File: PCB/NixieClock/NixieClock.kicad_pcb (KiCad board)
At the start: 2 copper layers, 1 part, among them U1 ESP32-DEVKITC-32D

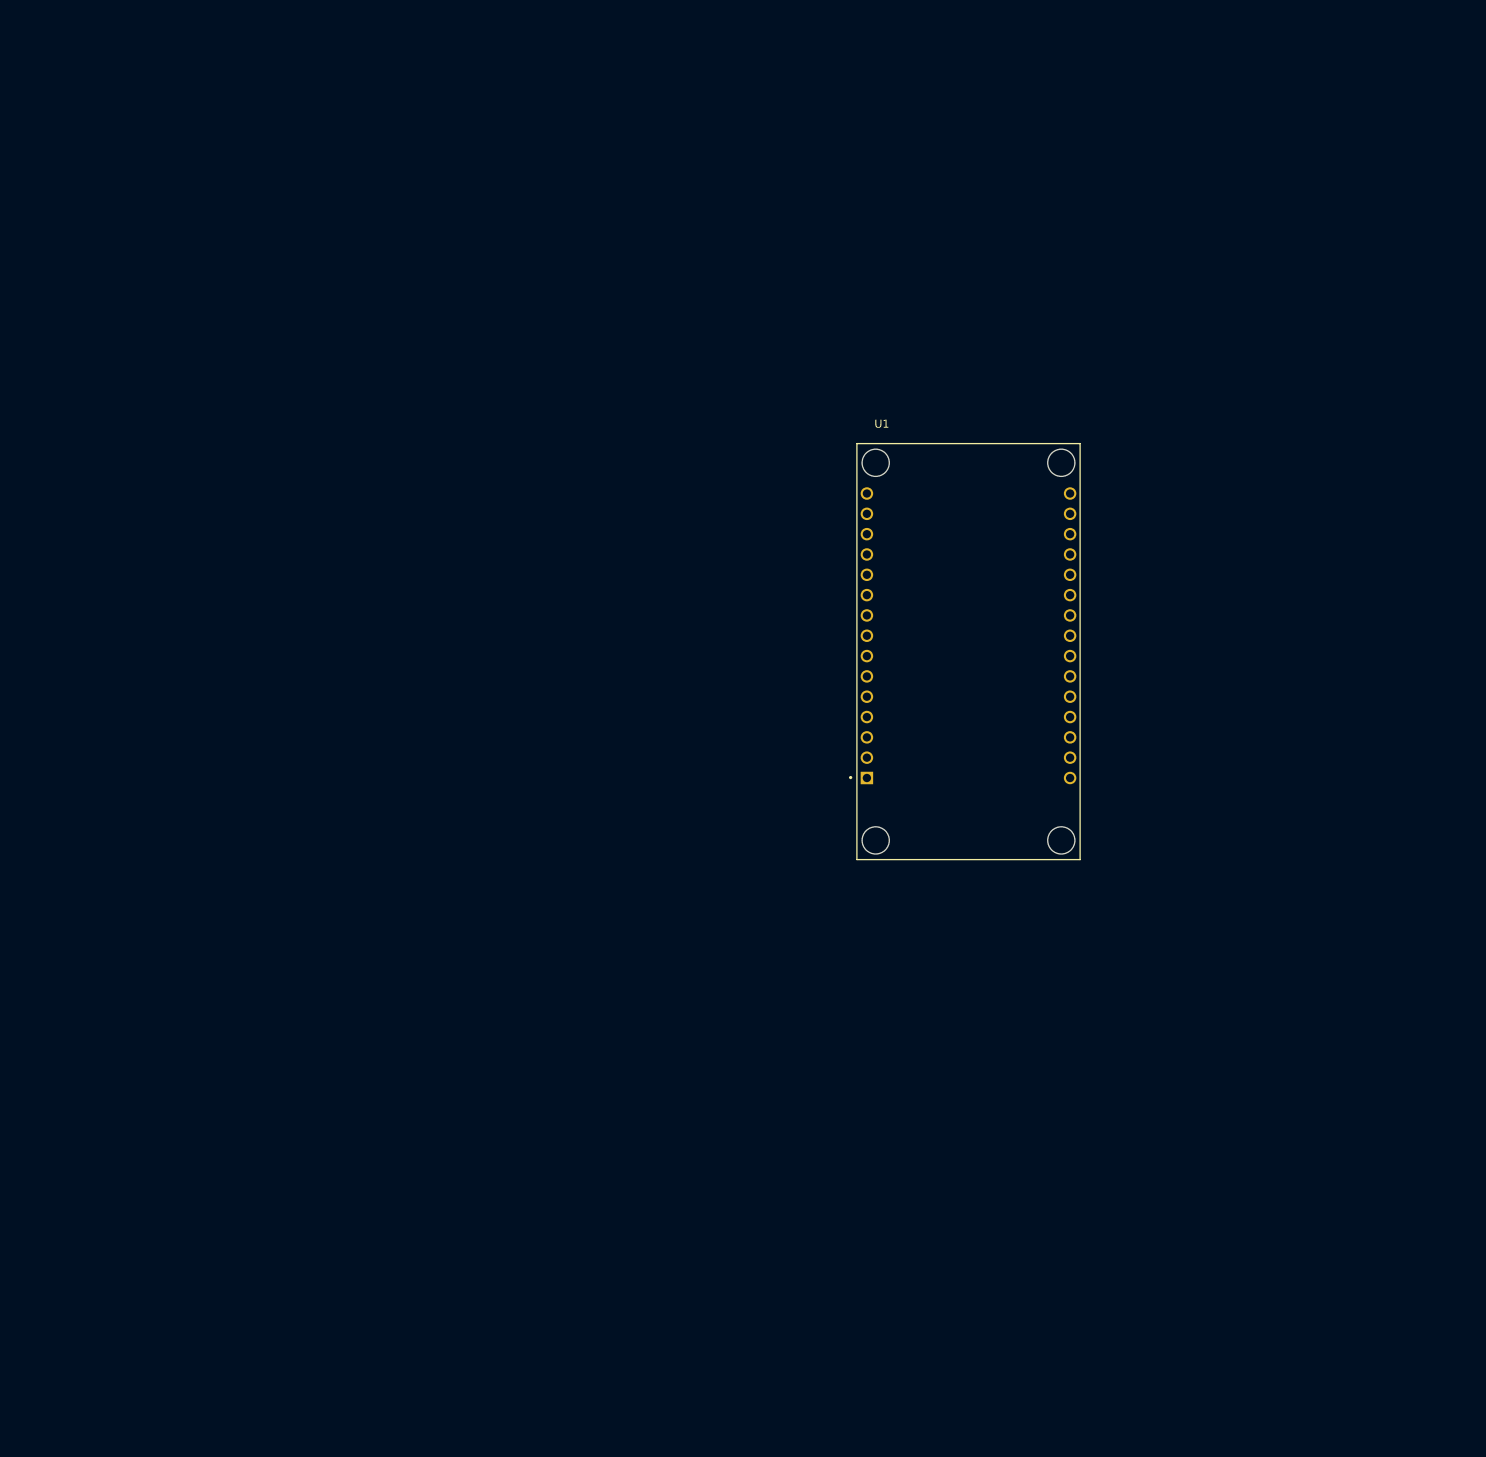
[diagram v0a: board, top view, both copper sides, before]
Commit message: nixie panel PCB layout progress
laid out tube 1 with top and bottom traces. added GND polygon on both sides, with exception zone around tube 1. tubes 2-4 to be laid out with top and bottom traces
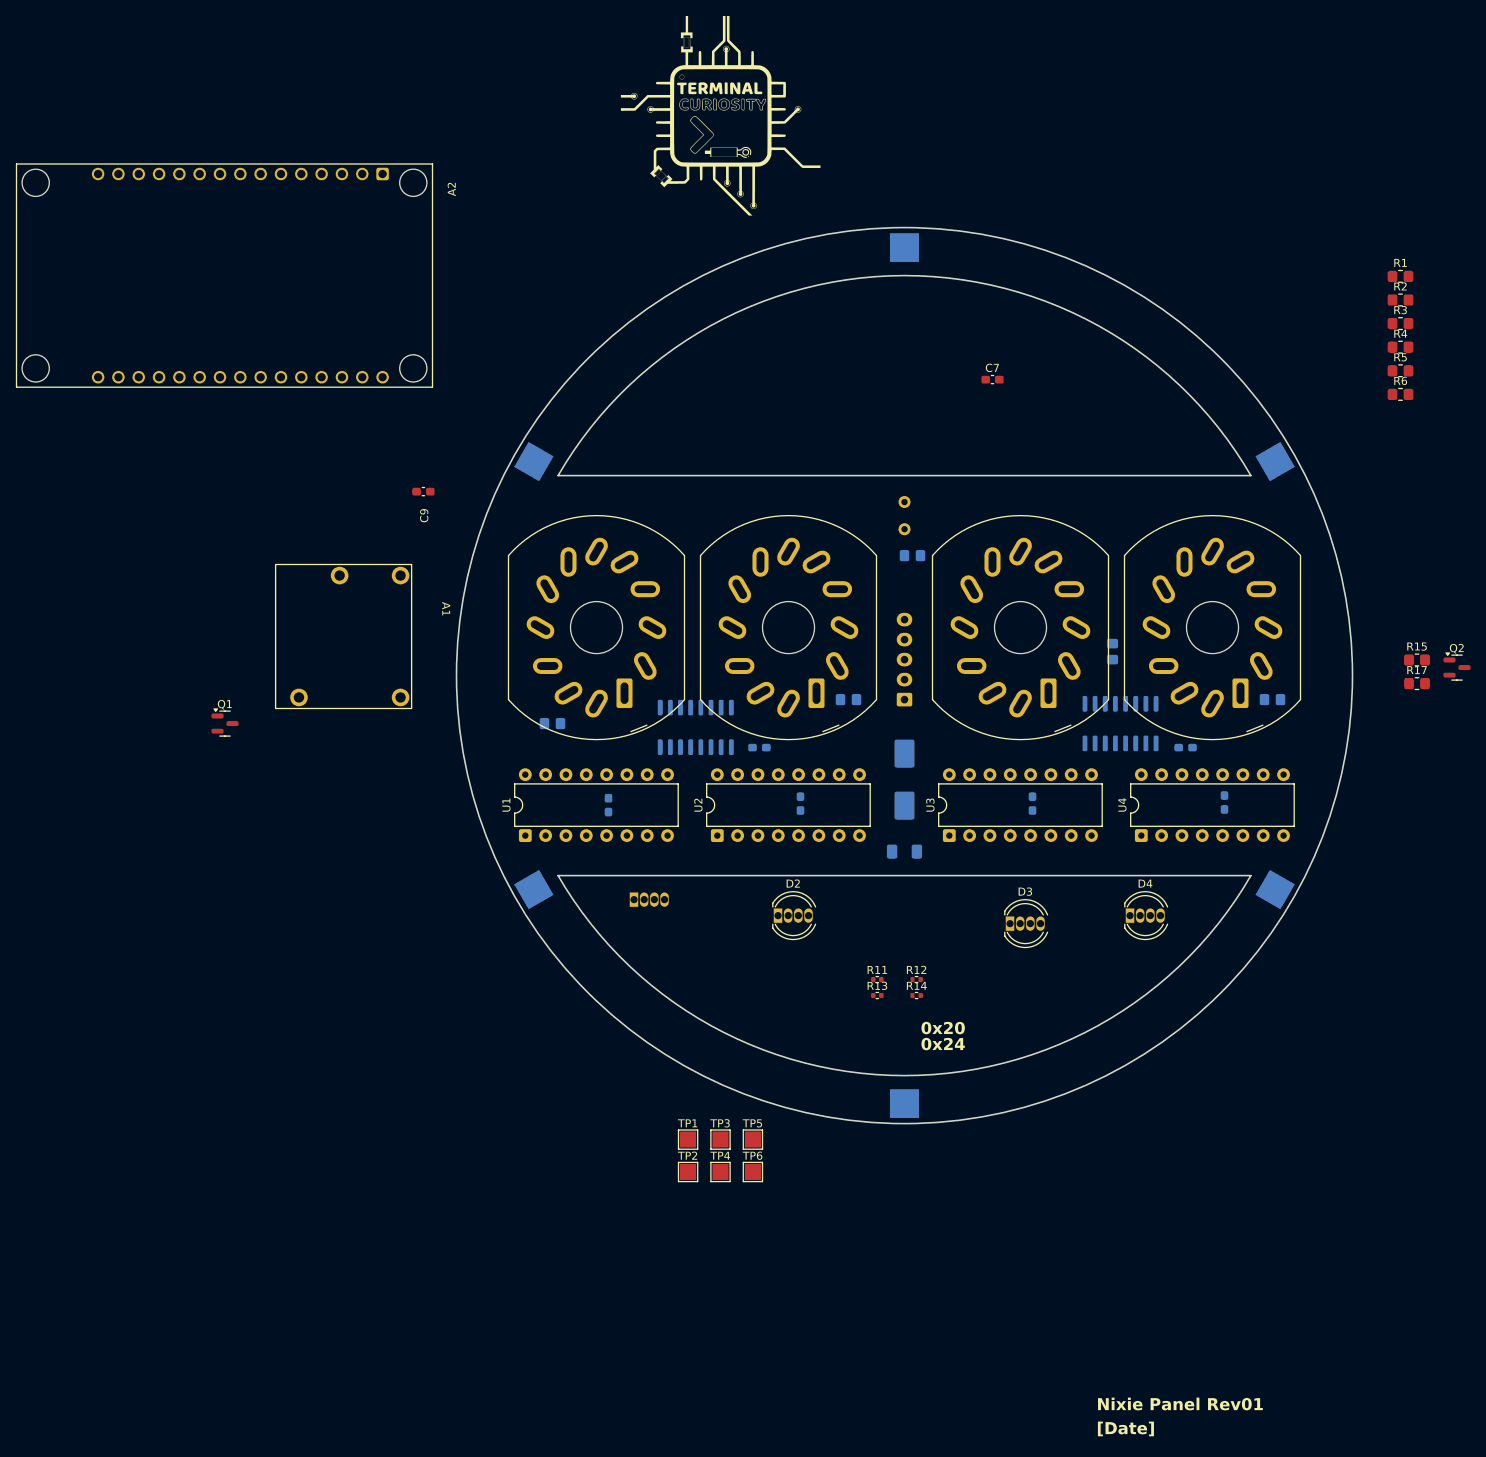
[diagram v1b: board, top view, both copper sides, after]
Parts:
- added A1: ASSY_NCH8200HV, TerminalCuriosityFootprints:NCH8200HV, F.Cu at (68.4, 86.1)
- added A2: IC_ESP32-WROOM-32_DEVKIT, TerminalCuriosityFootprints:MODULE_ESP32-DEVKITC-32D, F.Cu at (45.0, 50.0)
- added C1: 470uF, Capacitor_SMD:CP_Elec_8x10, B.Cu at (130.0, 113.0)
- added C2: 100nF, Capacitor_SMD:C_0603_1608Metric_Pad1.08x0.95mm_HandSolder, B.Cu at (165.1, 109.0)
- added C3: 100nF, Capacitor_SMD:C_0603_1608Metric_Pad1.08x0.95mm_HandSolder, B.Cu at (111.9, 109.0)
- added C4: 100nF, Capacitor_SMD:C_0603_1608Metric_Pad1.08x0.95mm_HandSolder, B.Cu at (170.0, 115.9)
- added C5: 100nF, Capacitor_SMD:C_0603_1608Metric_Pad1.08x0.95mm_HandSolder, B.Cu at (117.0, 116.0)
- added C6: 100nF, Capacitor_SMD:C_0603_1608Metric_Pad1.08x0.95mm_HandSolder, B.Cu at (146.0, 116.0)
- added C7: 100nF, Capacitor_SMD:C_0603_1608Metric_Pad1.08x0.95mm_HandSolder, F.Cu at (141.0, 63.0)
- added C8: 100nF, Capacitor_SMD:C_0603_1608Metric_Pad1.08x0.95mm_HandSolder, B.Cu at (93.0, 116.2)
- added C9: 100nF, Capacitor_SMD:C_0603_1608Metric_Pad1.08x0.95mm_HandSolder, F.Cu at (69.9, 77.0)
- added D1: LED_IN-RGB-PL9823, LED_THT:LED_D5.0mm-4_RGB, B.Cu at (96.2, 128.0)
- added D2: LED_IN-RGB-PL9823, LED_THT:LED_D5.0mm-4_RGB, F.Cu at (114.2, 130.0)
- added D3: LED_IN-RGB-PL9823, LED_THT:LED_D5.0mm-4_RGB, F.Cu at (143.2, 131.0)
- added D4: LED_IN-RGB-PL9823, LED_THT:LED_D5.0mm-4_RGB, F.Cu at (158.2, 130.0)
- added F1: 1.5A PTC, Resistor_SMD:R_1206_3216Metric_Pad1.30x1.75mm_HandSolder, B.Cu at (130.0, 122.0)
- added G1: LABEL_HVWarning, TerminalCuriosityFootprints:LABEL_HVWarning, B.Cu at (136.0, 33.2)
- added G2: LOGO, TerminalCuriosityFootprints:LABEL_TerminalCuriosity_25.0x25.0mm, F.Cu at (107.0, 30.0)
- added J1: Conn_01x05, Connector_JST:JST_XH_B5B-XH-A_1x05_P2.50mm_Vertical, B.Cu at (130.0, 103.0)
- added N1: TUBE_IN-12A_Nixie, TerminalCuriosityFootprints:in-12_nixie-tube, F.Cu at (91.5, 94.0)
- added N2: TUBE_IN-12A_Nixie, TerminalCuriosityFootprints:in-12_nixie-tube, F.Cu at (115.5, 94.0)
- added N3: TUBE_IN-12A_Nixie, TerminalCuriosityFootprints:in-12_nixie-tube, F.Cu at (144.5, 94.0)
- added N4: TUBE_IN-12A_Nixie, TerminalCuriosityFootprints:in-12_nixie-tube, F.Cu at (168.5, 94.0)
- added Q1: IRLML6244, Package_TO_SOT_SMD:SOT-23, F.Cu at (45.1, 106.0)
- added Q2: IRLML6244, Package_TO_SOT_SMD:SOT-23, F.Cu at (199.1, 99.0)
- added R1: 4.7K, Resistor_SMD:R_0805_2012Metric_Pad1.20x1.40mm_HandSolder, F.Cu at (192.0, 50.1)
- added R10: 18K, Resistor_SMD:R_0805_2012Metric_Pad1.20x1.40mm_HandSolder, B.Cu at (176.0, 103.0)
- added R11: 0R Netlink, Resistor_SMD:R_0402_1005Metric, F.Cu at (126.6, 138.0)
- added R12: 0R Netlink, Resistor_SMD:R_0402_1005Metric, F.Cu at (131.5, 138.0)
- added R13: 0R Netlink, Resistor_SMD:R_0402_1005Metric, F.Cu at (126.6, 140.0)
- added R14: 0R Netlink, Resistor_SMD:R_0402_1005Metric, F.Cu at (131.5, 140.0)
- added R15: 10k, Resistor_SMD:R_0805_2012Metric_Pad1.20x1.40mm_HandSolder, F.Cu at (194.1, 98.0)
- added R16: 10k, Resistor_SMD:R_0805_2012Metric_Pad1.20x1.40mm_HandSolder, B.Cu at (131.0, 85.0)
- added R17: 10k, Resistor_SMD:R_0805_2012Metric_Pad1.20x1.40mm_HandSolder, F.Cu at (194.1, 101.0)
- added R18: LDR07, OptoDevice:R_LDR_5.1x4.3mm_P3.4mm_Vertical, B.Cu at (130.0, 81.7)
- added R2: 4.7K, Resistor_SMD:R_0805_2012Metric_Pad1.20x1.40mm_HandSolder, F.Cu at (192.0, 53.0)
- added R3: 470R, Resistor_SMD:R_0805_2012Metric_Pad1.20x1.40mm_HandSolder, F.Cu at (192.0, 56.0)
- added R4: 10k, Resistor_SMD:R_0805_2012Metric_Pad1.20x1.40mm_HandSolder, F.Cu at (192.0, 59.0)
- added R5: 4.7K, Resistor_SMD:R_0805_2012Metric_Pad1.20x1.40mm_HandSolder, F.Cu at (192.0, 61.9)
- added R6: 4.7K, Resistor_SMD:R_0805_2012Metric_Pad1.20x1.40mm_HandSolder, F.Cu at (192.0, 64.8)
- added R7: 18K, Resistor_SMD:R_0805_2012Metric_Pad1.20x1.40mm_HandSolder, B.Cu at (86.0, 106.0)
- added R8: 18K, Resistor_SMD:R_0805_2012Metric_Pad1.20x1.40mm_HandSolder, B.Cu at (123.0, 103.0)
- added R9: 18K, Resistor_SMD:R_0805_2012Metric_Pad1.20x1.40mm_HandSolder, B.Cu at (156.0, 97.0)
- added TP1: TestPoint, TestPoint:TestPoint_Pad_2.0x2.0mm, F.Cu at (103.0, 158.0)
- added TP2: TestPoint, TestPoint:TestPoint_Pad_2.0x2.0mm, F.Cu at (103.0, 162.1)
- added TP3: TestPoint, TestPoint:TestPoint_Pad_2.0x2.0mm, F.Cu at (107.0, 158.0)
- added TP4: TestPoint, TestPoint:TestPoint_Pad_2.0x2.0mm, F.Cu at (107.0, 162.1)
- added TP5: TestPoint, TestPoint:TestPoint_Pad_2.0x2.0mm, F.Cu at (111.0, 158.0)
- added TP6: TestPoint, TestPoint:TestPoint_Pad_2.0x2.0mm, F.Cu at (111.0, 162.1)
- added U2: K155ID1, Package_DIP:DIP-16_W7.62mm, F.Cu at (106.6, 120.0)
- added U3: K155ID1, Package_DIP:DIP-16_W7.62mm, F.Cu at (135.6, 120.0)
- added U4: K155ID1, Package_DIP:DIP-16_W7.62mm, F.Cu at (159.6, 120.0)
- added U5: PCF8574, Package_SO:SOIC-16_3.9x9.9mm_P1.27mm, B.Cu at (103.9, 106.5)
- added U6: PCF8574, Package_SO:SOIC-16_3.9x9.9mm_P1.27mm, B.Cu at (157.0, 106.0)
- added X1: 5230, TerminalCuriosityFootprints:CONN-Batt-Spring-SMD-3.5mmX3.5mm, B.Cu at (176.3, 73.2)
- added X2: 5230, TerminalCuriosityFootprints:CONN-Batt-Spring-SMD-3.5mmX3.5mm, B.Cu at (130.0, 46.5)
- added X3: 5230, TerminalCuriosityFootprints:CONN-Batt-Spring-SMD-3.5mmX3.5mm, B.Cu at (83.7, 73.2)
- added X4: 5230, TerminalCuriosityFootprints:CONN-Batt-Spring-SMD-3.5mmX3.5mm, B.Cu at (83.7, 126.8)
- added X5: 5230, TerminalCuriosityFootprints:CONN-Batt-Spring-SMD-3.5mmX3.5mm, B.Cu at (130.0, 153.5)
- added X6: 5230, TerminalCuriosityFootprints:CONN-Batt-Spring-SMD-3.5mmX3.5mm, B.Cu at (176.3, 126.8)
- U1: value ESP32-DEVKITC-32D -> K155ID1; footprint ESP32-DEVKITC-32D:MODULE_ESP32-DEVKITC-32D -> Package_DIP:DIP-16_W7.62mm
- moved U1 60.0 mm to (82.6, 120.0), turned to 90 degrees
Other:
- board outline added: 112 x 112 mm
- board text added: "0x20"
- board text added: "0x24"
- board text added: "Nixie Panel Rev01"
- board text added: "[Date]"
